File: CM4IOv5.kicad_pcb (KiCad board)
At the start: 4 copper layers, 115.1 x 56 mm, 121 parts, among them J1 Conn_01x02, J10 HDMI_C_1.4, J11 HDMI_C_1.4, J12 Conn_02x07_Odd_Even, J13 Conn_01x03, J14 Conn_01x03, J15 Audio OUT, J16 Micro_SD_Card_Det, J17 THD-20-R, J2 Bus_M.2_Socket_B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

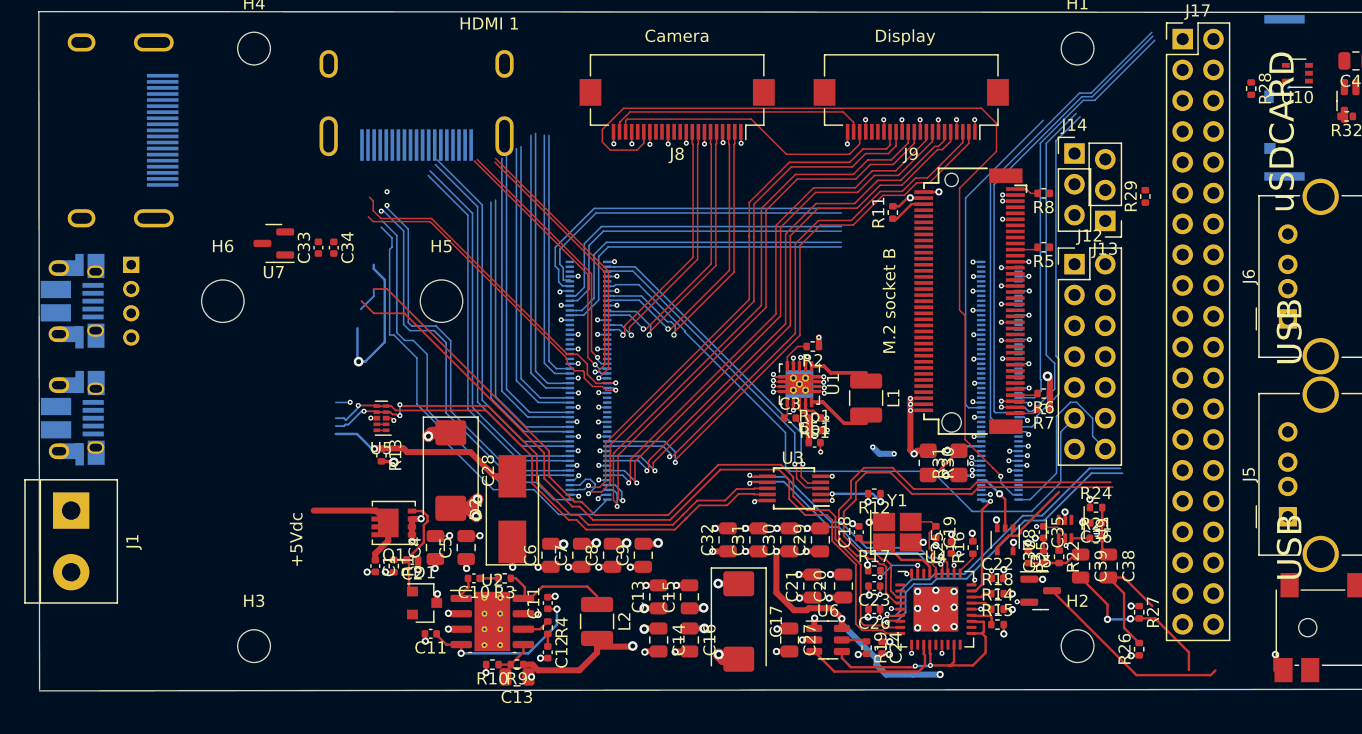
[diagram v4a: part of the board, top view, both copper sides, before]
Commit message: Routing High speed signals
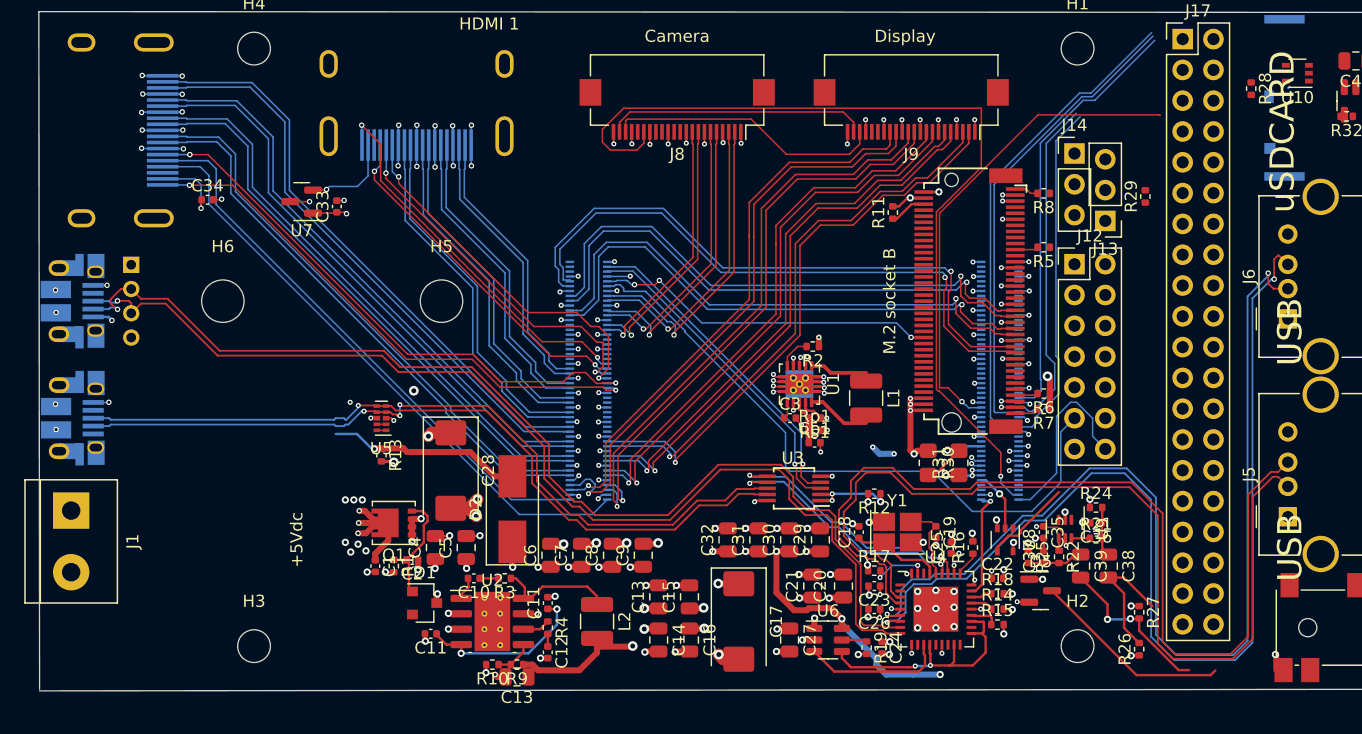
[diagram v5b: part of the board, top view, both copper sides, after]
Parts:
- moved C34 11.1 mm to (110.7, 94.5), turned to 0 degrees
- moved U7 4.15 mm to (118.5, 94.7)
- moved C33 3.72 mm to (121.4, 95.0)
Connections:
- net /CM4_HighSpeed/PCIE_CLK_nREQ renamed /PCIE_CLK_nREQ
- Module1 pad 109: /CM4_HighSpeed/PCIE_nRST -> /PCIE_nRST
- Module1 pad 110: /CM4_HighSpeed/PCIE_CLK_P -> /PCIE_CLK_P
- Module1 pad 112: /CM4_HighSpeed/PCIE_CLK_N -> /PCIE_CLK_N
- Module1 pad 116: /CM4_HighSpeed/PCIE_RX_P -> /PCIE_RX_P
- Module1 pad 118: /CM4_HighSpeed/PCIE_RX_N -> /PCIE_RX_N
- Module1 pad 122: /CM4_HighSpeed/PCIE_TX_P -> /PCIE_TX_P
- Module1 pad 124: /CM4_HighSpeed/PCIE_TX_N -> /PCIE_TX_N
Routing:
- net /+3.3vSSD: track 0.00 -> 86.6 mm, vias 0 -> 9
- net /+3.3v: track 318.5 -> 231.9 mm, vias 40 -> 30
- net Net-(J1-Pin_1): track 10.1 -> 83.3 mm, vias 0 -> 3
- net /USB2-HUB/HD3_P: track 26.6 -> 85.0 mm, vias 1 -> 2
- net /USB2-HUB/HD3_N: track 26.5 -> 84.1 mm, vias 1 -> 2
- net /USB2-HUB/VBUS: track 113.9 -> 166.0 mm, vias 8 -> 9
- net /PCIE_CLK_N: track 0.00 -> 50.9 mm, vias 0 -> 1
- net /PCIE_CLK_P: track 0.00 -> 49.6 mm, vias 0 -> 1
- net /CM4_HighSpeed/HDMI0_D1_P: track 0.00 -> 47.9 mm
- net /PCIE_RX_P: track 0.00 -> 46.0 mm, vias 0 -> 1
- net /PCIE_TX_P: track 0.00 -> 45.6 mm, vias 0 -> 1
- net /PCIE_RX_N: track 0.00 -> 45.2 mm, vias 0 -> 1
- net /PCIE_TX_N: track 0.00 -> 44.8 mm, vias 0 -> 1
- net /USB2-HUB/HD2_P: track 36.6 -> 76.6 mm
- net /USB2-HUB/HD2_N: track 35.5 -> 75.4 mm
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
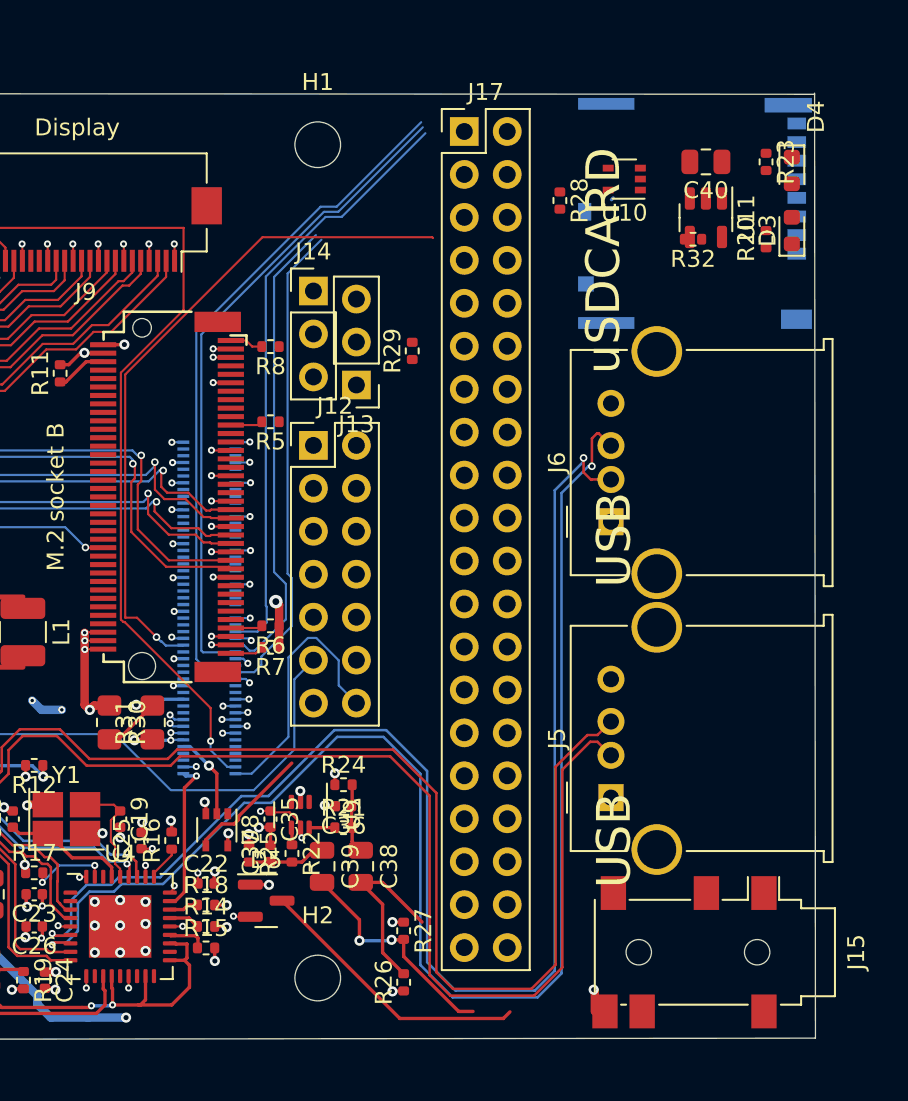
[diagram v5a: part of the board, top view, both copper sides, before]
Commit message: Routing SD
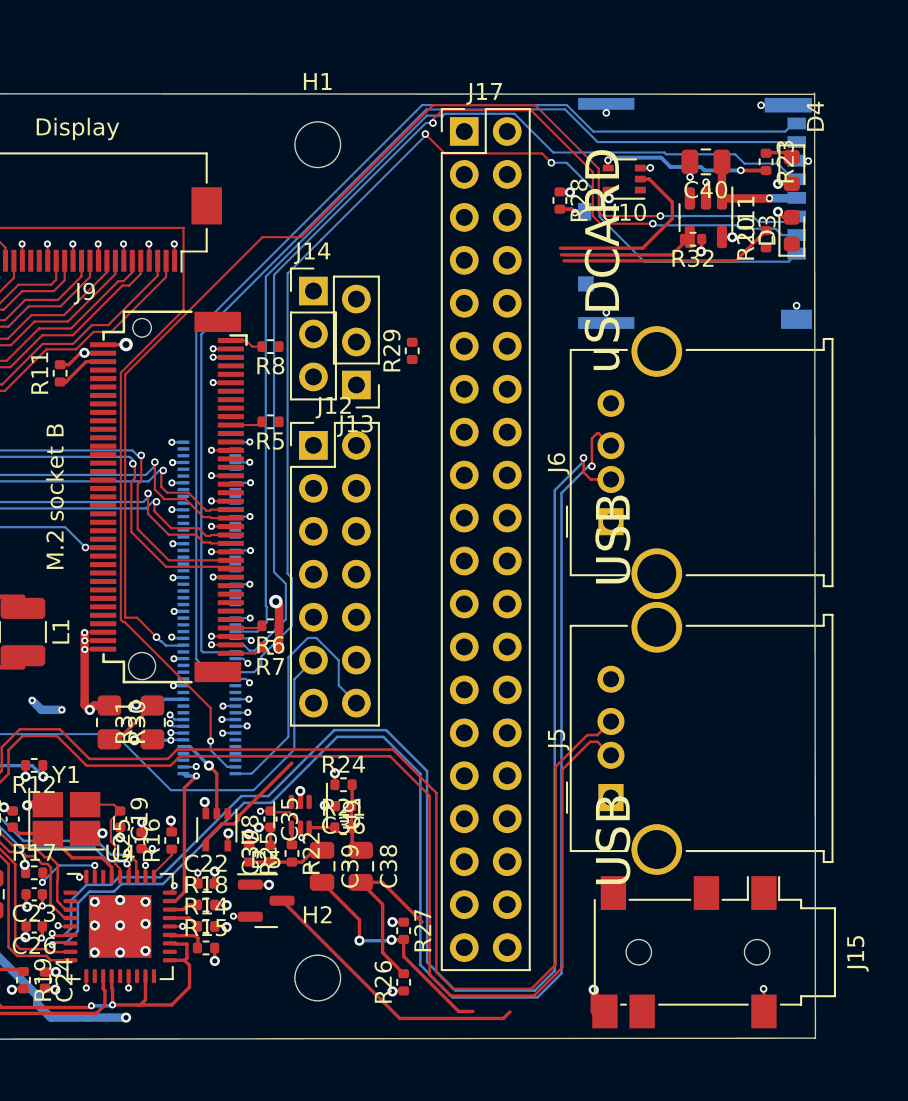
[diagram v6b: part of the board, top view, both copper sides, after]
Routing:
- net /+3.3v: track 231.9 -> 289.0 mm, vias 30 -> 36
- net /+5v: track 219.5 -> 268.0 mm
- net /CM4_GPIO (GPIO, SDCARD)/SD_DAT3: track 27.9 -> 64.2 mm, vias 0 -> 2
- net /CM4_GPIO (GPIO, SDCARD)/SD_DAT2: track 28.5 -> 63.3 mm, vias 0 -> 2
- net /CM4_GPIO (GPIO, SDCARD)/SD_CMD: track 40.1 -> 69.3 mm, vias 1 -> 2
- net /CM4_GPIO (GPIO, SDCARD)/SD_CLK: track 35.5 -> 59.6 mm
- net /CM4_GPIO (GPIO, SDCARD)/SD_DAT1: track 40.4 -> 63.9 mm
- net /CM4_GPIO (GPIO, SDCARD)/SD_DAT0: track 38.9 -> 62.3 mm
- net Net-(Module1A-PI_nLED_Activity): track 0.00 -> 12.7 mm
- net /CM4_GPIO (GPIO, SDCARD)/nPWR_LED: track 0.00 -> 10.8 mm
- net Net-(R23-Pad2): track 0.00 -> 10.2 mm, vias 0 -> 2
- net GND: track 170.0 -> 178.1 mm, vias 193 -> 202
- net /CM4_GPIO (GPIO, SDCARD)/SD_PWR_ON: track 0.01 -> 8.04 mm
- net /CM4_GPIO (GPIO, SDCARD)/SD_PWR: track 0.15 -> 6.60 mm, vias 0 -> 1
- net (no net): track 0.00 -> 2.65 mm
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
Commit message: Partialy routing GPIO
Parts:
- removed J12: Conn_02x07_Odd_Even, Connector_PinHeader_2.54mm:PinHeader_2x07_P2.54mm_Vertical
- moved J17 48.3 mm to (193.7, 129.5), turned to 180 degrees
- moved J14 19.4 mm to (186.6, 109.5)
- moved J13 13.5 mm to (182.8, 109.6), turned to 0 degrees
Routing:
- net /CM4_GPIO (GPIO, SDCARD)/nPWR_LED: track 10.8 -> 66.7 mm, vias 0 -> 1
- net /CM4_GPIO (GPIO, SDCARD)/TV_OUT: track 53.8 -> 0.00 mm
- net /CM4_GPIO (GPIO, SDCARD)/SD_PWR_ON: track 8.04 -> 55.1 mm, vias 0 -> 1
- net /CM4_GPIO (GPIO, SDCARD)/GPIO26: track 0.00 -> 39.0 mm, vias 0 -> 2
- net /CM4_GPIO (GPIO, SDCARD)/GPIO5: track 0.00 -> 38.2 mm, vias 0 -> 2
- net /CM4_GPIO (GPIO, SDCARD)/GPIO6: track 0.00 -> 37.3 mm, vias 0 -> 2
- net /CM4_GPIO (GPIO, SDCARD)/GPIO13: track 0.00 -> 37.1 mm, vias 0 -> 2
- net /CM4_GPIO (GPIO, SDCARD)/GPIO19: track 0.00 -> 37.0 mm, vias 0 -> 2
- net /+3.3v: track 289.0 -> 325.4 mm
- net /CM4_GPIO (GPIO, SDCARD)/Reserved: track 0.00 -> 34.8 mm, vias 0 -> 1
- net /CM4_GPIO (GPIO, SDCARD)/GPIO21: track 0.00 -> 33.7 mm
- net Net-(Module1A-PI_nLED_Activity): track 12.7 -> 46.2 mm, vias 0 -> 1
- net /CM4_GPIO (GPIO, SDCARD)/GPIO3: track 0.00 -> 29.4 mm, vias 0 -> 2
- net /CM4_GPIO (GPIO, SDCARD)/GPIO2: track 0.00 -> 29.4 mm, vias 0 -> 2
- net /+3.3vSSD: track 86.6 -> 115.6 mm, vias 9 -> 11
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
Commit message: All wires connected
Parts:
- moved C13 8.53 mm to (144.8, 133.0), turned to 0 degrees
- moved R9 0.35 mm to (136.3, 132.5)
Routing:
- net /CM4_GPIO (GPIO, SDCARD)/GPIO12: track 19.4 -> 56.3 mm, vias 2 -> 3
- net /CM4_GPIO (GPIO, SDCARD)/GPIO27: track 6.78 -> 38.8 mm
- net /CM4_GPIO (GPIO, SDCARD)/GPIO13: track 37.1 -> 64.7 mm, vias 2 -> 3
- net /CM4_GPIO (GPIO, SDCARD)/GPIO17: track 8.69 -> 35.2 mm
- net /CM4_GPIO (GPIO, SDCARD)/GPIO15: track 7.77 -> 30.4 mm, vias 1 -> 2
- net Net-(D2-A): track 16.6 -> 36.6 mm
- net /CM4_GPIO (GPIO, SDCARD)/GPIO23: track 0.00 -> 16.5 mm, vias 0 -> 1
- net /CM4_GPIO (GPIO, SDCARD)/GPIO18: track 5.62 -> 21.4 mm, vias 1 -> 3
- net /CM4_GPIO (GPIO, SDCARD)/GPIO22: track 6.01 -> 21.3 mm
- net /CM4_GPIO (GPIO, SDCARD)/GPIO10: track 8.29 -> 23.1 mm
- net /CM4_GPIO (GPIO, SDCARD)/GPIO24: track 2.25 -> 15.1 mm
- net /CM4_GPIO (GPIO, SDCARD)/GPIO25: track 6.00 -> 16.8 mm, vias 1 -> 2
- net /CM4_GPIO (GPIO, SDCARD)/GPIO14: track 17.3 -> 28.1 mm
- net /CM4_GPIO (GPIO, SDCARD)/GPIO8: track 7.67 -> 17.3 mm, vias 1 -> 2
- net /CM4_GPIO (GPIO, SDCARD)/GPIO11: track 13.7 -> 23.0 mm
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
